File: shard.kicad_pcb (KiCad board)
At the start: 2 copper layers, 151.2 x 102.5 mm, 61 parts, among them J1 Audio-Jack-4, M2 MountingHole_2.2mm_M2, U1 ARDUINO_PRO_MICRO

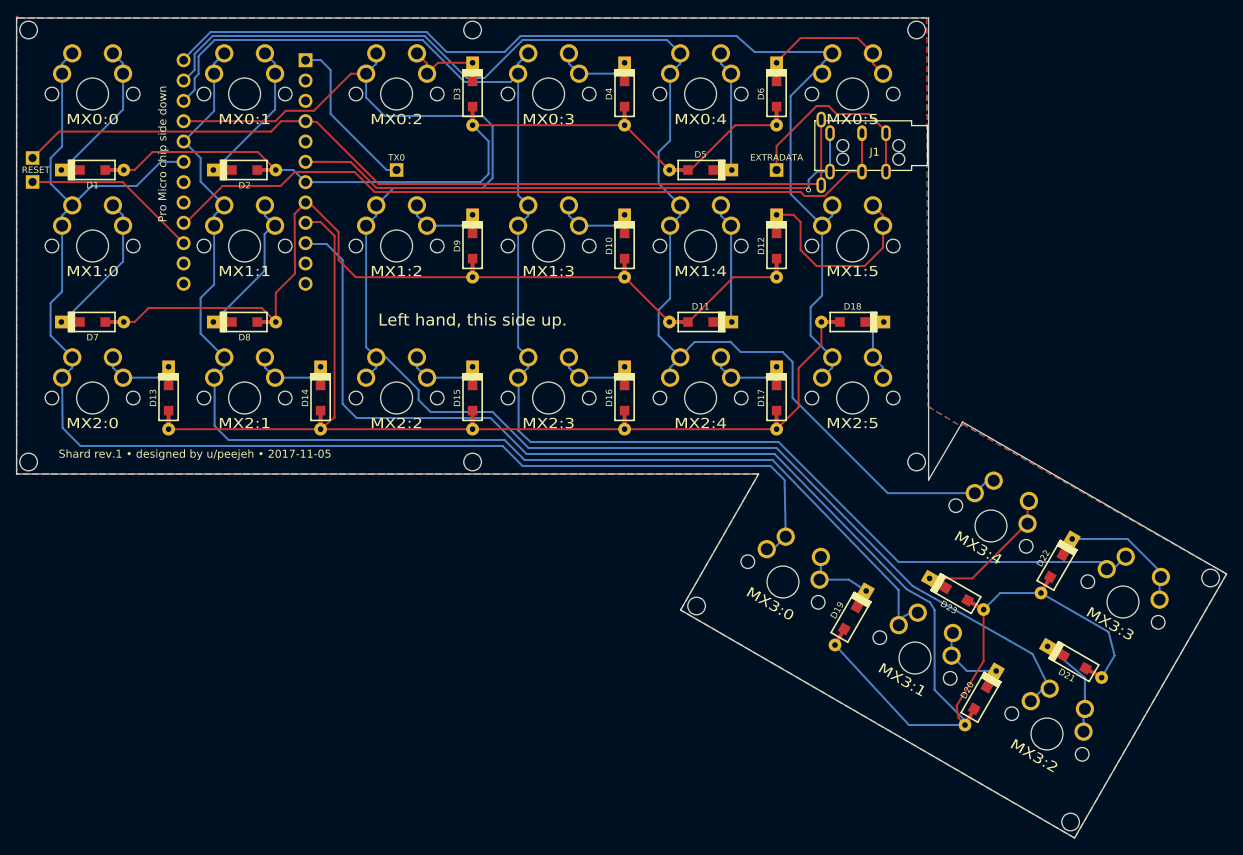
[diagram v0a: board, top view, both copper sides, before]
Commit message: Add holes for standoffs and re-route
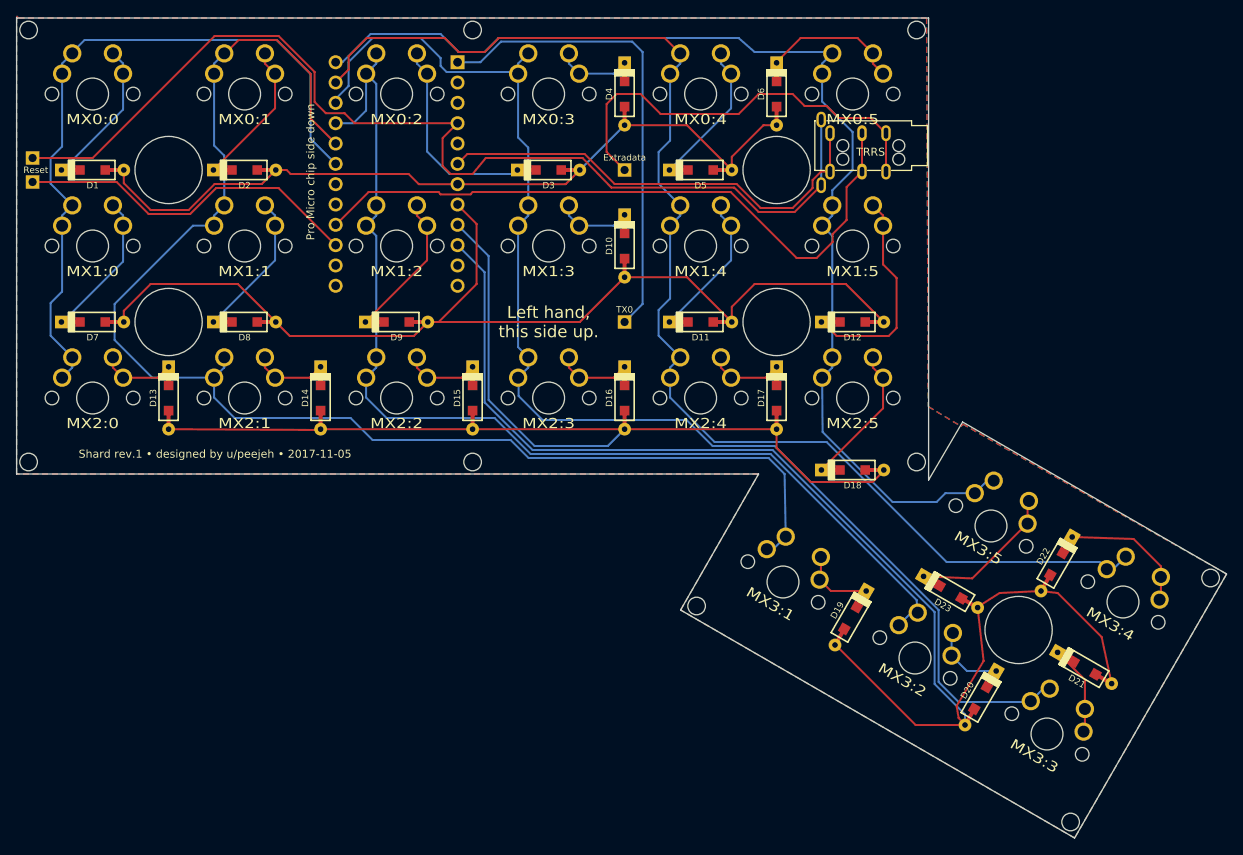
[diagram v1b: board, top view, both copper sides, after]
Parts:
- added M8: MountingHole_8.4mm_M8, Mounting_Holes:MountingHole_8.4mm_M8, F.Cu at (204.8, 125.0)
- added M8: MountingHole_8.4mm_M8, Mounting_Holes:MountingHole_8.4mm_M8, F.Cu at (174.5, 67.5)
- added M8: MountingHole_8.4mm_M8, Mounting_Holes:MountingHole_8.4mm_M8, F.Cu at (98.5, 67.5)
- added M8: MountingHole_8.4mm_M8, Mounting_Holes:MountingHole_8.4mm_M8, F.Cu at (98.5, 86.5)
- added M8: MountingHole_8.4mm_M8, Mounting_Holes:MountingHole_8.4mm_M8, F.Cu at (174.5, 86.5)
- EXTRADATA1: value EXTRADATA -> Extradata
- GROUND1: value Conn_01x01 -> Ground
- J1: value Audio-Jack-4 -> TRRS
- MX3:1: renamed from MX3:0; value MX3:11 -> MX3:10
- MX3:2: renamed from MX3:1; value MX3:10 -> MX3:9
- MX3:3: renamed from MX3:2; value MX3:9 -> MX3:8
- MX3:4: renamed from MX3:3; value MX3:8 -> MX3:7
- MX3:5: renamed from MX3:4; value MX3:7 -> MX3:6
- RESET1: value RESET -> Reset
- TX0: value Conn_01x01 -> TX0
- moved TX0 34.3 mm to (155.5, 86.5)
- moved U1 19.0 mm to (127.0, 68.0)
- moved EXTRADATA1 19.0 mm to (155.5, 67.5)
- moved D18 18.5 mm to (184.0, 105.0), turned to 0 degrees
- moved D12 13.4 mm to (184.0, 86.5), turned to 0 degrees
- moved D3 13.4 mm to (146.0, 67.5), turned to 0 degrees
- moved D9 13.4 mm to (127.0, 86.5), turned to 0 degrees
- moved D21 1.46 mm to (213.0, 129.8)
- moved D23 0.79 mm to (196.2, 120.2)
- moved D22 0.25 mm to (209.5, 116.8)
- turned D11 to 0 degrees
- turned D5 to 0 degrees
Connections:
- MX3:1 pad 1: /Col0 -> /Col1
- MX3:2 pad 1: /Col1 -> /Col2
- MX3:3 pad 1: /Col2 -> /Col3
- MX3:4 pad 1: /Col3 -> /Col4
- MX3:5 pad 1: /Col4 -> /Col5
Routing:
- net /Col0: track 171.2 -> 90.5 mm
- net /Col2: track 199.0 -> 138.7 mm
- net Net-(TX0-Pad1): track 20.3 -> 59.4 mm
- net Net-(EXTRADATA1-Pad1): track 25.1 -> 53.5 mm
- net /Row1: track 106.3 -> 132.3 mm
- net Net-(RESET1-Pad1): track 22.1 -> 43.8 mm
- net GND: track 112.0 -> 133.4 mm
- net /Row3: track 184.5 -> 164.6 mm
- net /Col1: track 154.2 -> 173.5 mm
- net /Col3: track 183.5 -> 164.5 mm
- net /Row2: track 121.1 -> 138.0 mm
- net Net-(J1-Pad1): track 73.5 -> 57.2 mm, vias 1 -> 0
- net Net-(D3-Pad1): track 9.32 -> 25.5 mm
- net VCC: track 94.7 -> 83.5 mm
- net Net-(D18-Pad1): track 8.05 -> 17.9 mm
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
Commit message: Move M2 mounting holes in from board edge
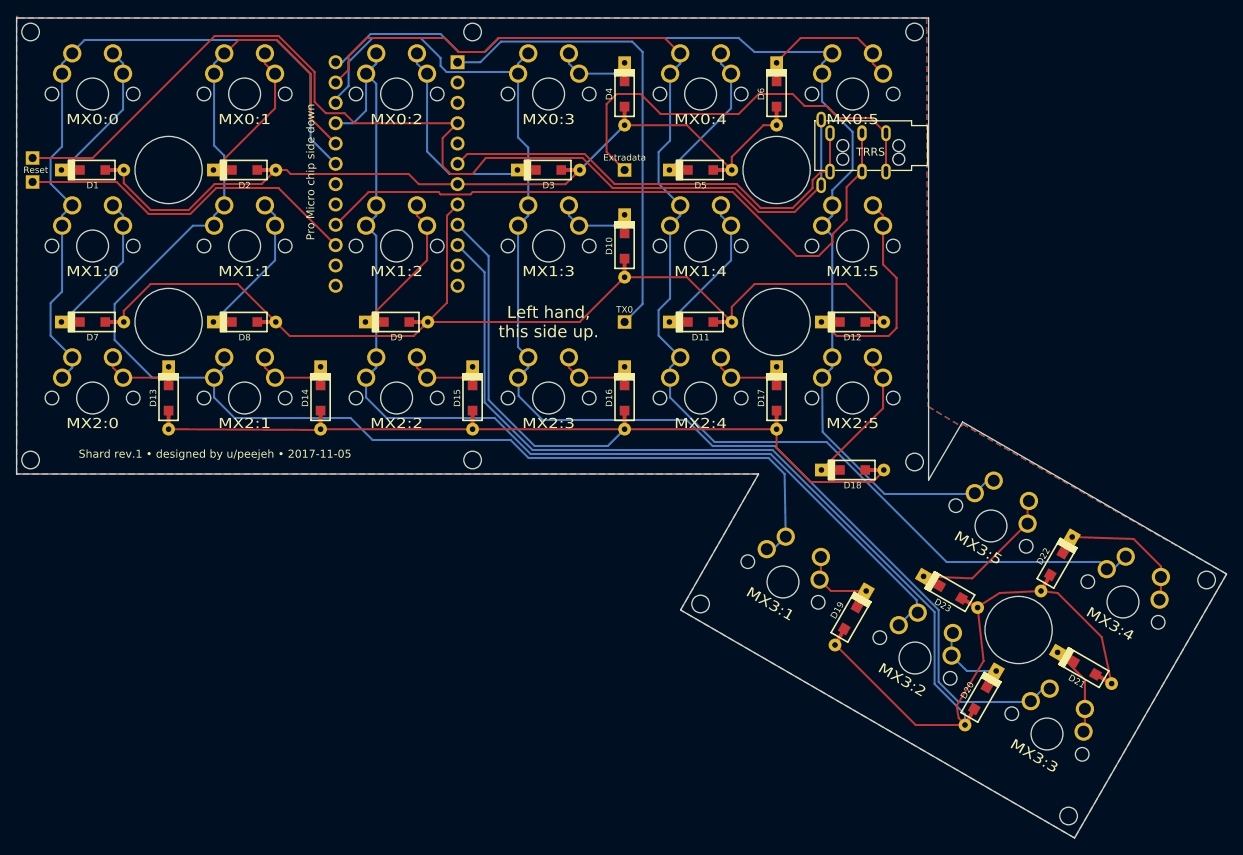
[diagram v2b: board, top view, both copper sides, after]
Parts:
- moved M2 0.79 mm to (211.0, 148.2)
- moved M2 0.56 mm to (165.0, 121.8)
- moved M2 0.56 mm to (228.2, 118.8)
- moved M2 0.35 mm to (191.8, 50.2)
- moved M2 0.35 mm to (81.2, 50.2)
- moved M2 0.35 mm to (81.2, 103.8)
- moved M2 0.25 mm to (136.5, 50.2)
- moved M2 0.25 mm to (191.8, 104.0)
- moved M2 0.25 mm to (136.5, 103.8)
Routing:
- net /Row1: track 132.3 -> 129.6 mm
- net /Col5: track 144.1 -> 143.2 mm

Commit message: Re-align diodes
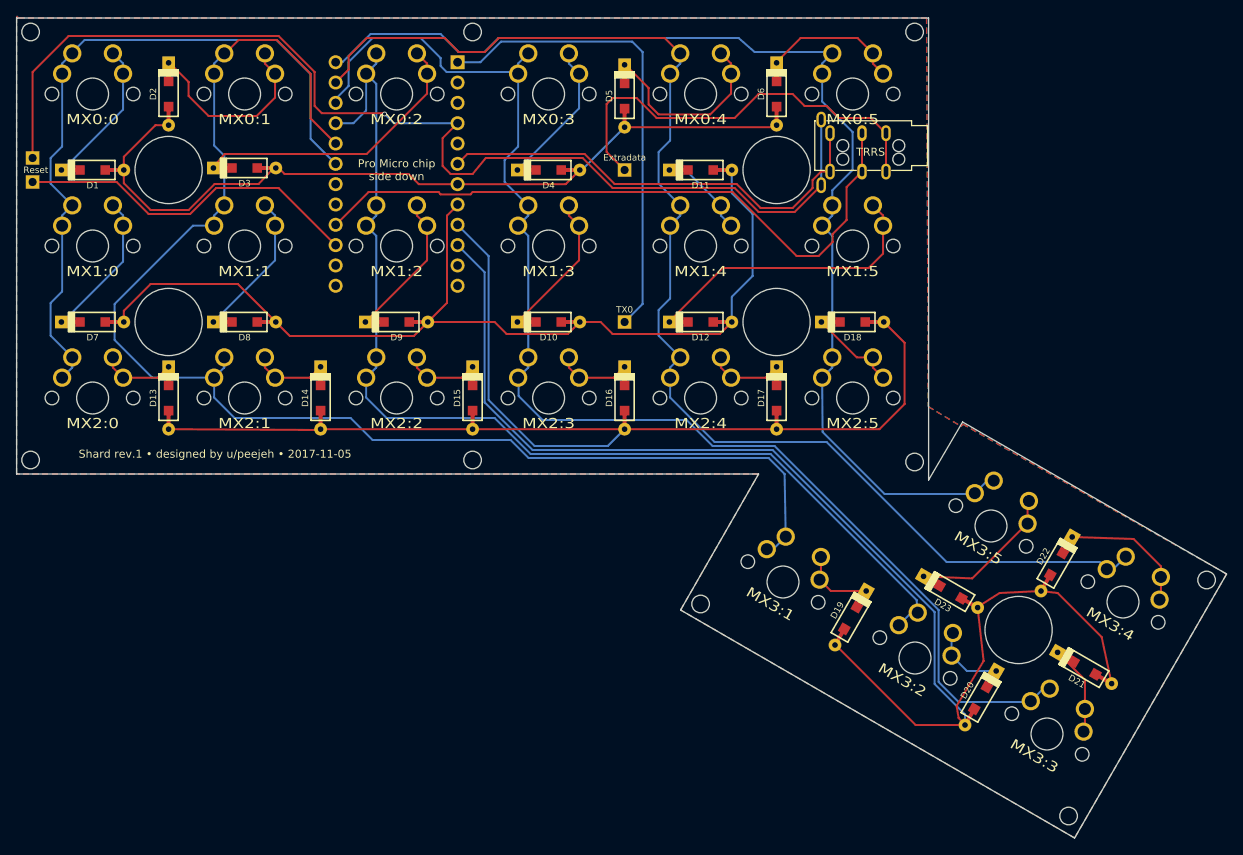
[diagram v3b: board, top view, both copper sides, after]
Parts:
- moved D3 38.0 mm to (108.0, 67.2)
- moved D11 19.0 mm to (165.0, 67.5)
- moved D12 19.0 mm to (165.0, 86.5)
- moved D18 18.5 mm to (184.0, 86.5)
- moved D10 13.4 mm to (146.0, 86.5), turned to 0 degrees
- moved D2 13.4 mm to (98.5, 58.0), turned to 270 degrees
- moved D4 13.4 mm to (146.0, 67.5), turned to 0 degrees
- moved D5 13.3 mm to (155.5, 58.2), turned to 270 degrees
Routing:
- net Net-(D3-Pad1): track 25.5 -> 36.3 mm
- net /Row2: track 138.0 -> 148.4 mm
- net Net-(D12-Pad1): track 27.2 -> 36.9 mm
- net Net-(D10-Pad1): track 9.32 -> 18.3 mm
- net Net-(D4-Pad1): track 9.32 -> 18.3 mm
- net Net-(D11-Pad1): track 18.4 -> 11.3 mm
- net GND: track 133.4 -> 139.9 mm, vias 0 -> 1
- net Net-(D18-Pad1): track 17.9 -> 11.6 mm
- net Net-(D2-Pad1): track 18.4 -> 24.1 mm
- net Net-(D5-Pad1): track 18.4 -> 23.7 mm
- net /Row1: track 129.6 -> 124.9 mm
- net /Col3: track 164.5 -> 165.9 mm
- net /Row0: track 99.5 -> 100.3 mm
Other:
- board text removed: "Left hand, this side up."
- board text removed: "Right hand, this side up."

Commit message: Move TRRS away from switches to improve clearance
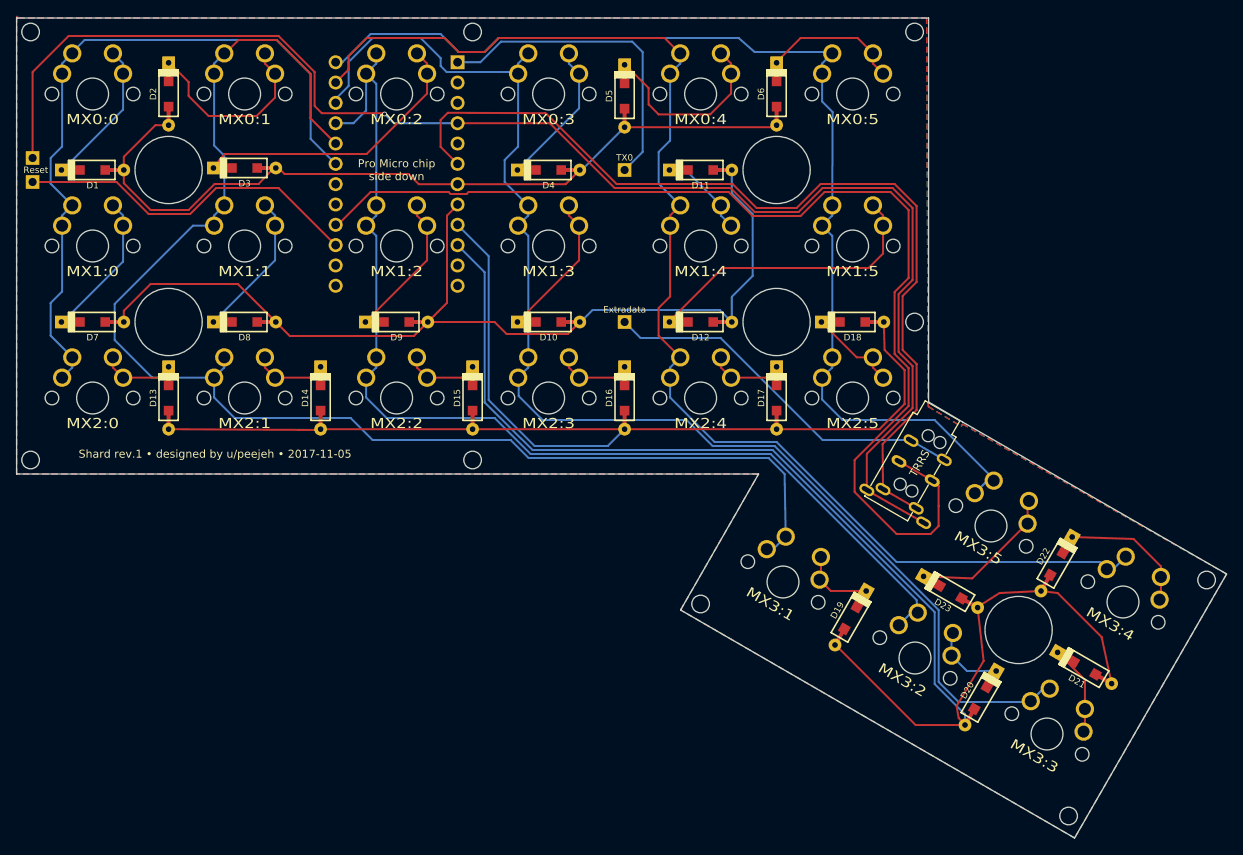
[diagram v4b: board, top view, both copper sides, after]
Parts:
- moved J1 40.6 mm to (191.8, 105.2), turned to 240 degrees
- moved EXTRADATA1 19.0 mm to (155.5, 86.5)
- moved TX0 19.0 mm to (155.5, 67.5)
- moved M2 17.5 mm to (191.8, 86.5)
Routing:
- net Net-(J1-Pad1): track 57.2 -> 116.9 mm
- net VCC: track 83.3 -> 140.4 mm
- net GND: track 139.9 -> 183.6 mm
- net Net-(TX0-Pad1): track 59.4 -> 40.4 mm
- net Net-(EXTRADATA1-Pad1): track 53.5 -> 46.7 mm
- net /Col5: track 143.2 -> 140.7 mm
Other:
- outline, holes or cut-outs redrawn

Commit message: Adjust Pro Micro pinout to match Let's Split
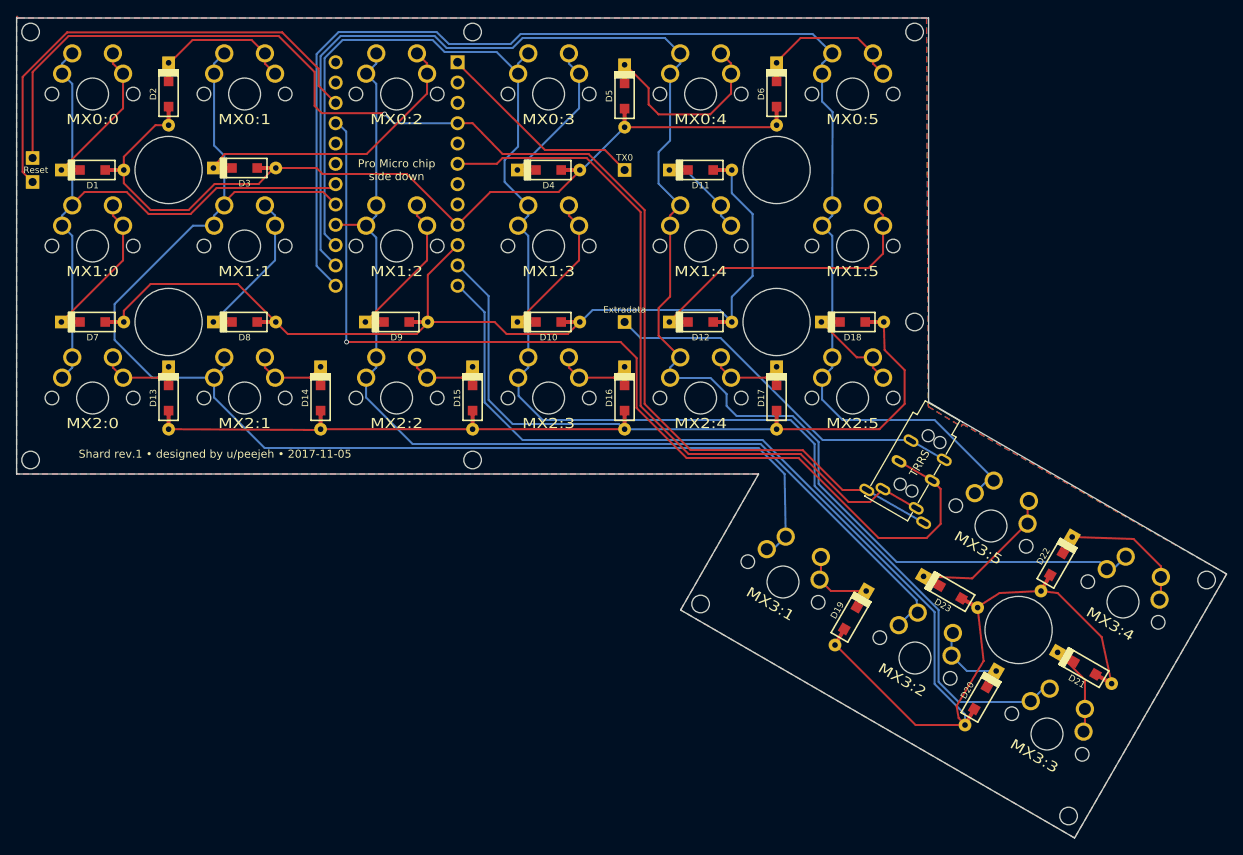
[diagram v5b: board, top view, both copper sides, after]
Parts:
- U1: footprint keebs:Pro_Micro -> footprints:ARDUINO_PRO_MICRO
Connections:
- U1 pad 10: /Row3 -> /Row1
- U1 pad 11: Net-(U1-Pad11) -> /Row2
- U1 pad 12: Net-(U1-Pad12) -> /Row3
- U1 pad 7: /Row0 -> Net-(U1-Pad7)
- U1 pad 8: /Row1 -> Net-(U1-Pad8)
- U1 pad 9: /Row2 -> /Row0
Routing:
- net /Col5: track 140.7 -> 172.4 mm
- net /Col4: track 163.2 -> 192.0 mm
- net Net-(J1-Pad1): track 116.9 -> 91.0 mm
- net /Col3: track 165.9 -> 189.2 mm
- net GND: track 183.6 -> 165.3 mm
- net Net-(RESET1-Pad1): track 43.8 -> 60.0 mm
- net Net-(TX0-Pad1): track 40.4 -> 26.5 mm
- net VCC: track 140.4 -> 127.5 mm, vias 0 -> 1
- net /Col0: track 90.5 -> 79.7 mm
- net /Col1: track 173.5 -> 165.7 mm
- net Net-(D2-Pad1): track 24.1 -> 17.1 mm
- net /Row2: track 148.4 -> 141.6 mm
- net /Row1: track 124.9 -> 119.6 mm
- net /Col2: track 138.7 -> 133.6 mm
- net /Row3: track 164.6 -> 159.6 mm
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
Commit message: Add case base to plate PCB
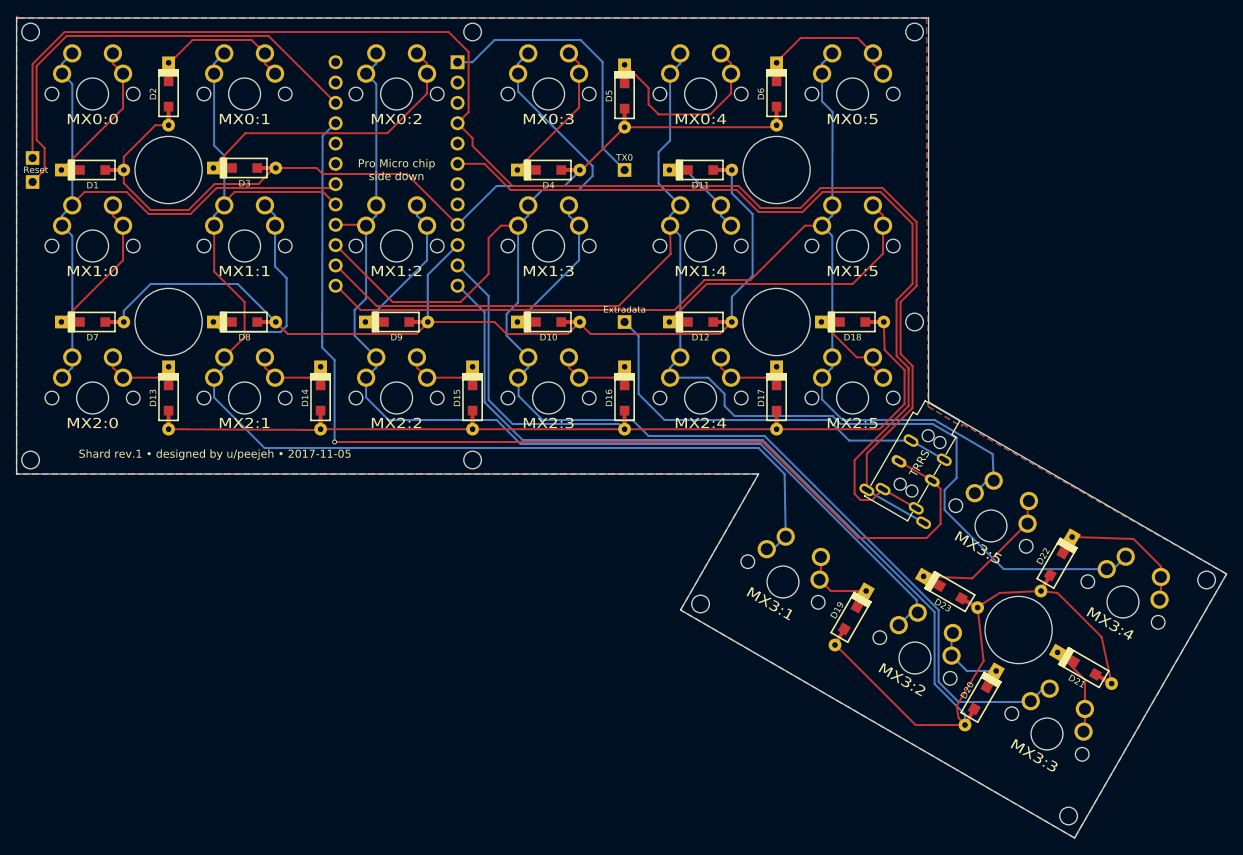
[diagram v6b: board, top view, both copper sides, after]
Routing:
- net /Col5: track 172.4 -> 142.3 mm
- net GND: track 165.3 -> 189.1 mm, vias 1 -> 0
- net /Col4: track 192.0 -> 170.2 mm
- net Net-(J1-Pad1): track 91.0 -> 109.3 mm
- net /Col1: track 165.7 -> 149.4 mm
- net /Col3: track 189.2 -> 176.7 mm
- net Net-(TX0-Pad1): track 26.5 -> 35.1 mm
- net Net-(D8-Pad1): track 18.3 -> 26.2 mm
- net VCC: track 127.5 -> 133.4 mm
- net Net-(EXTRADATA1-Pad1): track 46.7 -> 51.0 mm
- net Net-(RESET1-Pad1): track 60.0 -> 57.9 mm
- net /Col2: track 133.6 -> 135.1 mm
